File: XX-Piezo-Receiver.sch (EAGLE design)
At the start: 10 parts, among them IC1 TL072D, IC2 L78LXXBD/CD, J1 AVR_SPI_PROG_3X2PTH, U1 ATMEGA1284P-AU

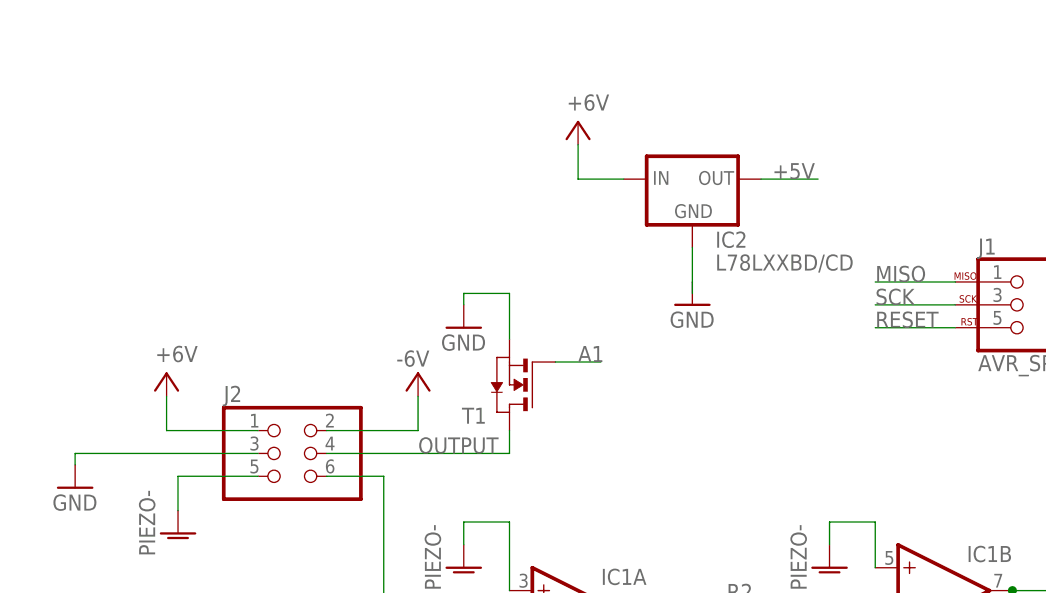
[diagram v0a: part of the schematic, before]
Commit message: Added decoupling caps and mount hole.
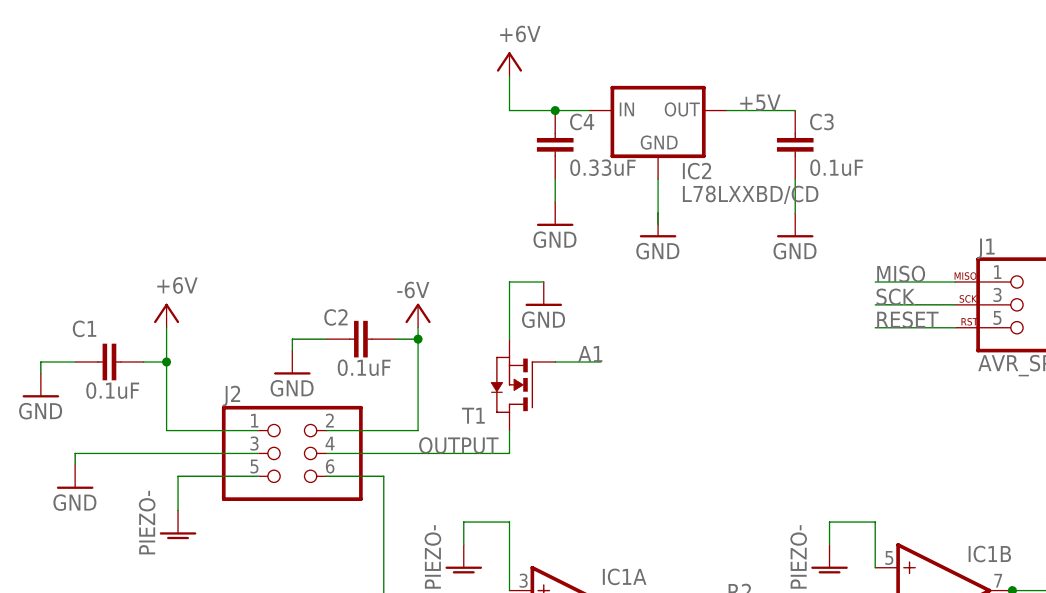
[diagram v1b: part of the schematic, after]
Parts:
- added C1, C2, C3: 0.1uF, rcl:C-EUC0402
- added C4: 0.33uF, rcl:C-EUC0402
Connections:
- net +5V: now also C3.1
- net +6V: now also C1.2, C4.1
- net -6V: now also C2.2
- net GND: now also C1.1, C2.1, C3.2, C4.2, IC2.GND2, IC2.GND3, IC2.GND4
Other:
- moved on the sheet: IC2
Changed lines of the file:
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@@
 <?xml version="1.0" encoding="utf-8"?>
 <!DOCTYPE eagle SYSTEM "eagle.dtd">
-<eagle version="8.3.2">
+<eagle version="8.7.0">
 <drawing>
 <settings>
@@
 <setting verticaltext="up"/>
 </settings>
-<grid distance="50" unitdist="mil" unit="mil" style="lines" multiple="1" display="yes" altdistance="0.01" altunitdist="inch" altunit="inch"/>
+<grid distance="50" unitdist="mil" unit="mil" style="dots" multiple="1" display="yes" altdistance="0.01" altunitdist="inch" altunit="inch"/>
 <layers>
 <layer number="1" name="Top" color="4" fill="1" visible="no" active="no"/>
@@
 <part name="T1" library="zetex" library_urn="urn:adsk.eagle:library:418" deviceset="NMOSSOT23" device="" package3d_urn="urn:adsk.eagle:package:30981/1"/>
 <part name="+6V1" library="supply2" library_urn="urn:adsk.eagle:library:372" deviceset="V+" device="" value="+6V"/>
+<part name="C1" library="rcl" library_urn="urn:adsk.eagle:library:334" deviceset="C-EU" device="C0402" package3d_urn="urn:adsk.eagle:package:23626/1" value="0.1uF"/>
+<part name="C2" library="rcl" library_urn="urn:adsk.eagle:library:334" deviceset="C-EU" device="C0402" package3d_urn="urn:adsk.eagle:package:23626/1" value="0.1uF"/>
+<part name="GND6" library="supply1" library_urn="urn:adsk.eagle:library:371" deviceset="GND" device=""/>
+<part name="C3" library="rcl" library_urn="urn:adsk.eagle:library:334" deviceset="C-EU" device="C0402" package3d_urn="urn:adsk.eagle:package:23626/1" value="0.1uF"/>
+<part name="GND7" library="supply1" library_urn="urn:adsk.eagle:library:371" deviceset="GND" device=""/>
+<part name="GND8" library="supply1" library_urn="urn:adsk.eagle:library:371" deviceset="GND" device=""/>
+<part name="C4" library="rcl" library_urn="urn:adsk.eagle:library:334" deviceset="C-EU" device="C0402" package3d_urn="urn:adsk.eagle:package:23626/1" value="0.33uF"/>
+<part name="GND9" library="supply1" library_urn="urn:adsk.eagle:library:371" deviceset="GND" device=""/>
 </parts>
 <sheets>
@@
 <instance part="IC1" gate="A" x="27.94" y="60.96"/>
 <instance part="IC1" gate="B" x="68.58" y="63.5"/>
-<instance part="-6V" gate="1" x="10.16" y="87.63" rot="R180"/>
-<instance part="+6V" gate="1" x="-17.78" y="87.63"/>
+<instance part="-6V" gate="1" x="10.16" y="95.25" rot="R180"/>
+<instance part="+6V" gate="1" x="-17.78" y="95.25"/>
 <instance part="GND1" gate="1" x="-27.94" y="74.93"/>
 <instance part="GND2" gate="1" x="99.06" y="13.97"/>
@@
 <instance part="R4" gate="G$1" x="63.5" y="50.8"/>
 <instance part="GND3" gate="1" x="96.52" y="87.63"/>
-<instance part="GND4" gate="1" x="15.24" y="92.71"/>
-<instance part="IC2" gate="G$1" x="40.64" y="109.22"/>
-<instance part="GND5" gate="1" x="40.64" y="95.25"/>
+<instance part="GND4" gate="1" x="24.13" y="95.25"/>
+<instance part="IC2" gate="G$1" x="36.83" y="116.84"/>
+<instance part="GND5" gate="1" x="36.83" y="102.87"/>
 <instance part="T1" gate="A" x="20.32" y="86.36" rot="R180"/>
-<instance part="+6V1" gate="1" x="27.94" y="115.57"/>
+<instance part="+6V1" gate="1" x="20.32" y="123.19"/>
+<instance part="C1" gate="G$1" x="-25.4" y="88.9" smashed="yes" rot="R90">
+<attribute name="NAME" x="-28.321" y="91.694" size="1.778" layer="95"/>
+<attribute name="VALUE" x="-20.701" y="86.614" size="1.778" layer="96" rot="R180"/>
+</instance>
+<instance part="C2" gate="G$1" x="2.54" y="91.44" smashed="yes" rot="R90">
+<attribute name="NAME" x="-0.381" y="92.964" size="1.778" layer="95"/>
+<attribute name="VALUE" x="7.239" y="89.154" size="1.778" layer="96" rot="R180"/>
+</instance>
+<instance part="GND6" gate="1" x="52.07" y="102.87"/>
+<instance part="C3" gate="G$1" x="52.07" y="114.3"/>
+<instance part="GND7" gate="1" x="-31.75" y="85.09"/>
+<instance part="GND8" gate="1" x="-3.81" y="87.63"/>
+<instance part="C4" gate="G$1" x="25.4" y="114.3"/>
+<instance part="GND9" gate="1" x="25.4" y="104.14"/>
 </instances>
 <busses>
@@
 <segment>
 <pinref part="IC2" gate="G$1" pin="OUT"/>
-<wire x1="48.26" y1="109.22" x2="54.61" y2="109.22" width="0.1524" layer="91"/>
-<label x="49.53" y="109.22" size="1.778" layer="95"/>
+<wire x1="44.45" y1="116.84" x2="52.07" y2="116.84" width="0.1524" layer="91"/>
+<label x="45.72" y="116.84" size="1.778" layer="95"/>
+<pinref part="C3" gate="G$1" pin="1"/>
 </segment>
 </net>
@@
 <pinref part="+6V" gate="1" pin="V+"/>
 <wire x1="-7.62" y1="81.28" x2="-17.78" y2="81.28" width="0.1524" layer="91"/>
-<wire x1="-17.78" y1="81.28" x2="-17.78" y2="85.09" width="0.1524" layer="91"/>
+<wire x1="-17.78" y1="81.28" x2="-17.78" y2="88.9" width="0.1524" layer="91"/>
+<pinref part="C1" gate="G$1" pin="2"/>
+<wire x1="-17.78" y1="88.9" x2="-17.78" y2="92.71" width="0.1524" layer="91"/>
+<wire x1="-17.78" y1="88.9" x2="-20.32" y2="88.9" width="0.1524" layer="91"/>
+<junction x="-17.78" y="88.9"/>
 </segment>
 <segment>
 <pinref part="IC2" gate="G$1" pin="IN"/>
-<wire x1="33.02" y1="109.22" x2="27.94" y2="109.22" width="0.1524" layer="91"/>
+<wire x1="29.21" y1="116.84" x2="25.4" y2="116.84" width="0.1524" layer="91"/>
 <pinref part="+6V1" gate="1" pin="V+"/>
-<wire x1="27.94" y1="109.22" x2="27.94" y2="113.03" width="0.1524" layer="91"/>
+<wire x1="25.4" y1="116.84" x2="20.32" y2="116.84" width="0.1524" layer="91"/>
+<wire x1="20.32" y1="116.84" x2="20.32" y2="120.65" width="0.1524" layer="91"/>
+<pinref part="C4" gate="G$1" pin="1"/>
+<junction x="25.4" y="116.84"/>
 </segment>
 </net>
@@
 <pinref part="-6V" gate="1" pin="V-"/>
 <wire x1="0" y1="81.28" x2="10.16" y2="81.28" width="0.1524" layer="91"/>
-<wire x1="10.16" y1="81.28" x2="10.16" y2="85.09" width="0.1524" layer="91"/>
+<wire x1="10.16" y1="81.28" x2="10.16" y2="91.44" width="0.1524" layer="91"/>
+<pinref part="C2" gate="G$1" pin="2"/>
+<wire x1="10.16" y1="91.44" x2="10.16" y2="92.71" width="0.1524" layer="91"/>
+<wire x1="10.16" y1="91.44" x2="7.62" y2="91.44" width="0.1524" layer="91"/>
+<junction x="10.16" y="91.44"/>
 </segment>
 </net>
@@
 </segment>
 <segment>
-<wire x1="20.32" y1="91.44" x2="20.32" y2="96.52" width="0.1524" layer="91"/>
-<wire x1="20.32" y1="96.52" x2="15.24" y2="96.52" width="0.1524" layer="91"/>
+<wire x1="20.32" y1="91.44" x2="20.32" y2="97.79" width="0.1524" layer="91"/>
 <pinref part="GND4" gate="1" pin="GND"/>
-<wire x1="15.24" y1="96.52" x2="15.24" y2="95.25" width="0.1524" layer="91"/>
+<wire x1="20.32" y1="97.79" x2="24.13" y2="97.79" width="0.1524" layer="91"/>
 <pinref part="T1" gate="A" pin="S"/>
 </segment>
 <segment>
+<pinref part="GND5" gate="1" pin="GND"/>
+<wire x1="36.83" y1="105.41" x2="36.83" y2="104.14" width="0.1524" layer="91"/>
 <pinref part="IC2" gate="G$1" pin="GND1"/>
-<wire x1="40.64" y1="101.6" x2="40.64" y2="97.79" width="0.1524" layer="91"/>
-<pinref part="GND5" gate="1" pin="GND"/>
-<wire x1="40.64" y1="97.79" x2="40.64" y2="96.52" width="0.1524" layer="91"/>
+<pinref part="IC2" gate="G$1" pin="GND2"/>
+<pinref part="IC2" gate="G$1" pin="GND3"/>
+<pinref part="IC2" gate="G$1" pin="GND4"/>
+<wire x1="36.83" y1="109.22" x2="36.83" y2="105.41" width="0.1524" layer="91"/>
+</segment>
+<segment>
+<pinref part="C3" gate="G$1" pin="2"/>
+<wire x1="52.07" y1="109.22" x2="52.07" y2="105.41" width="0.1524" layer="91"/>
+<pinref part="GND6" gate="1" pin="GND"/>
+</segment>
+<segment>
+<pinref part="C1" gate="G$1" pin="1"/>
+<pinref part="GND7" gate="1" pin="GND"/>
+<wire x1="-27.94" y1="88.9" x2="-31.75" y2="88.9" width="0.1524" layer="91"/>
+<wire x1="-31.75" y1="88.9" x2="-31.75" y2="87.63" width="0.1524" layer="91"/>
+</segment>
+<segment>
+<pinref part="C2" gate="G$1" pin="1"/>
+<pinref part="GND8" gate="1" pin="GND"/>
+<wire x1="0" y1="91.44" x2="-3.81" y2="91.44" width="0.1524" layer="91"/>
+<wire x1="-3.81" y1="91.44" x2="-3.81" y2="90.17" width="0.1524" layer="91"/>
+</segment>
+<segment>
+<pinref part="C4" gate="G$1" pin="2"/>
+<pinref part="GND9" gate="1" pin="GND"/>
+<wire x1="25.4" y1="109.22" x2="25.4" y2="106.68" width="0.1524" layer="91"/>
 </segment>
 </net>
@@
 packages will not be understood (or retained) with this version.
 </note>
+<note version="8.4" severity="warning">
+Since Version 8.4, EAGLE supports properties for SPICE simulation.
+Probes in schematics and SPICE mapping objects found in parts and library devices
+will not be understood with this version. Update EAGLE to the latest version
+for full support of SPICE simulation.
+</note>
 </compatibility>

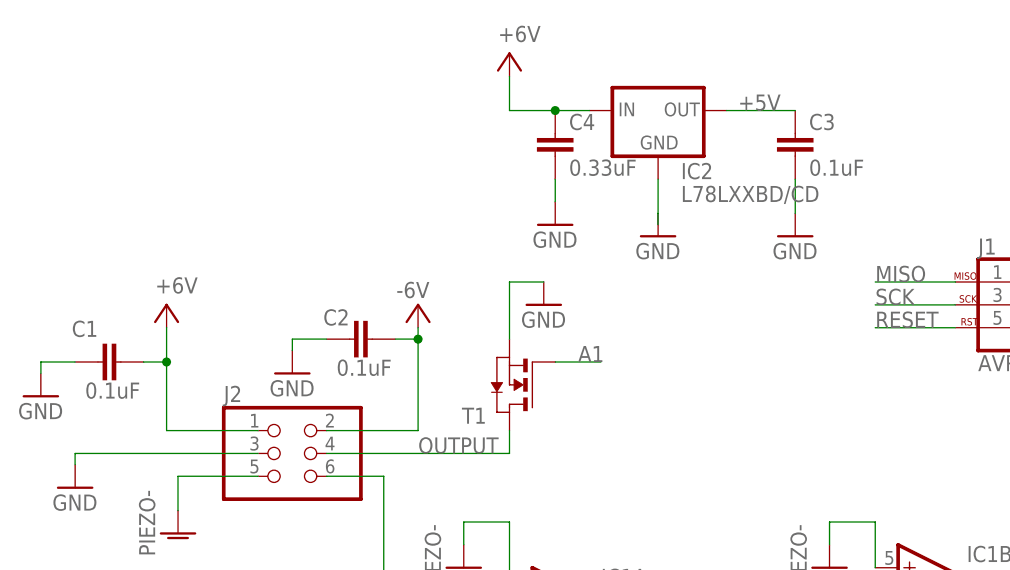
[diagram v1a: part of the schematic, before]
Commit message: Change to 0603 components. Add new lin reg. Add new mount hole.
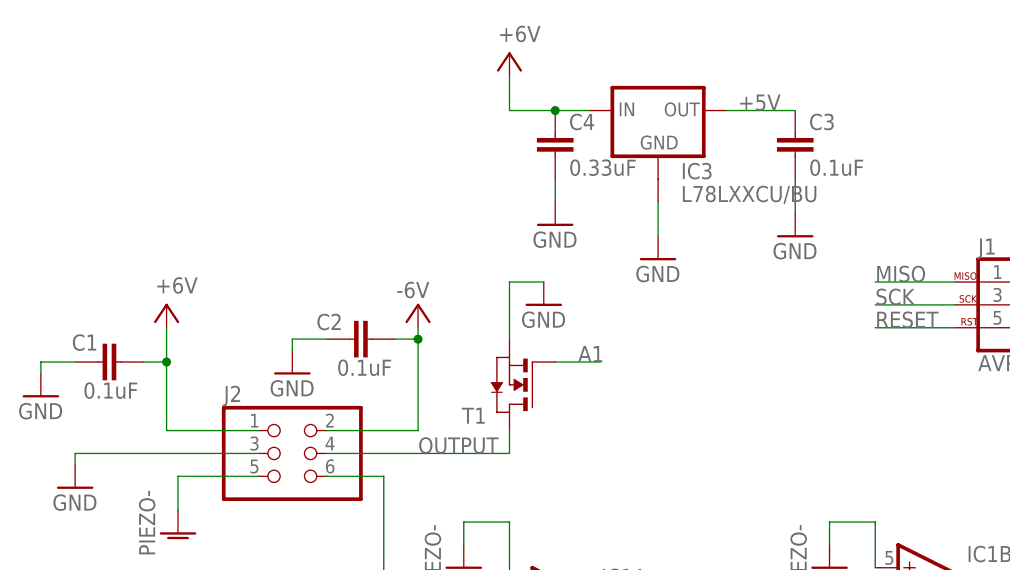
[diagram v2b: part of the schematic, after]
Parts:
- removed IC2: L78LXXBD/CD, v-reg-3:L78LXXBD/CD
- added IC3: L78LXXCU/BU, v-reg-3:L78LXXCU/BU
- C1, C2, C3, C4: device rcl:C-EUC0402 -> rcl:C-EUC0603
- R1, R2, R3, R4: device rcl:R-US_R0402 -> rcl:R-US_R0603
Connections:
- net +5V: now also IC3.OUT; no longer IC2.OUT
- net +6V: now also IC3.IN; no longer IC2.IN
- net GND: now also IC3.GND1; no longer IC2.GND1, IC2.GND2, IC2.GND3, IC2.GND4
